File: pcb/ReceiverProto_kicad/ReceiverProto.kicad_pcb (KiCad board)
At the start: 4 copper layers, 75 x 50 mm, 65 parts, among them J1 Conn_01x09, J2 Conn_01x03, J3 Conn_01x04, J4 Conn_01x06, U11 ADM8660ARZ-REEL, U12 ADP7182AUJZ-1.8-R7, U13 ADA4807-1, U14 ADA4807-1, U15 ADA4807-1, U16 ADA4807-1, U4 AD7387BCPZ-RL7, U5 TLV9001IDCK, U6 TLV9001IDCK, U7 TPS79301DBVR

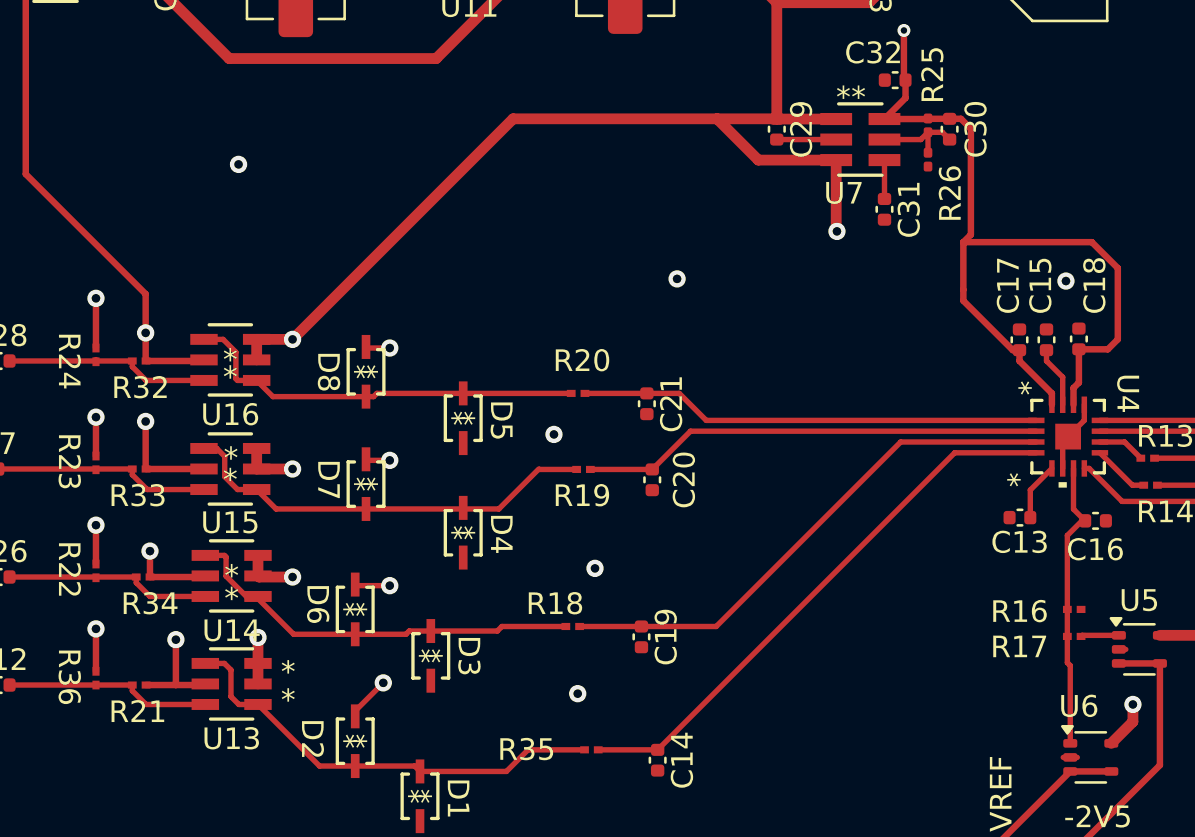
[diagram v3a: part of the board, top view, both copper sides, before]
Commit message: fixed all DRC errors except for silkscreen error.
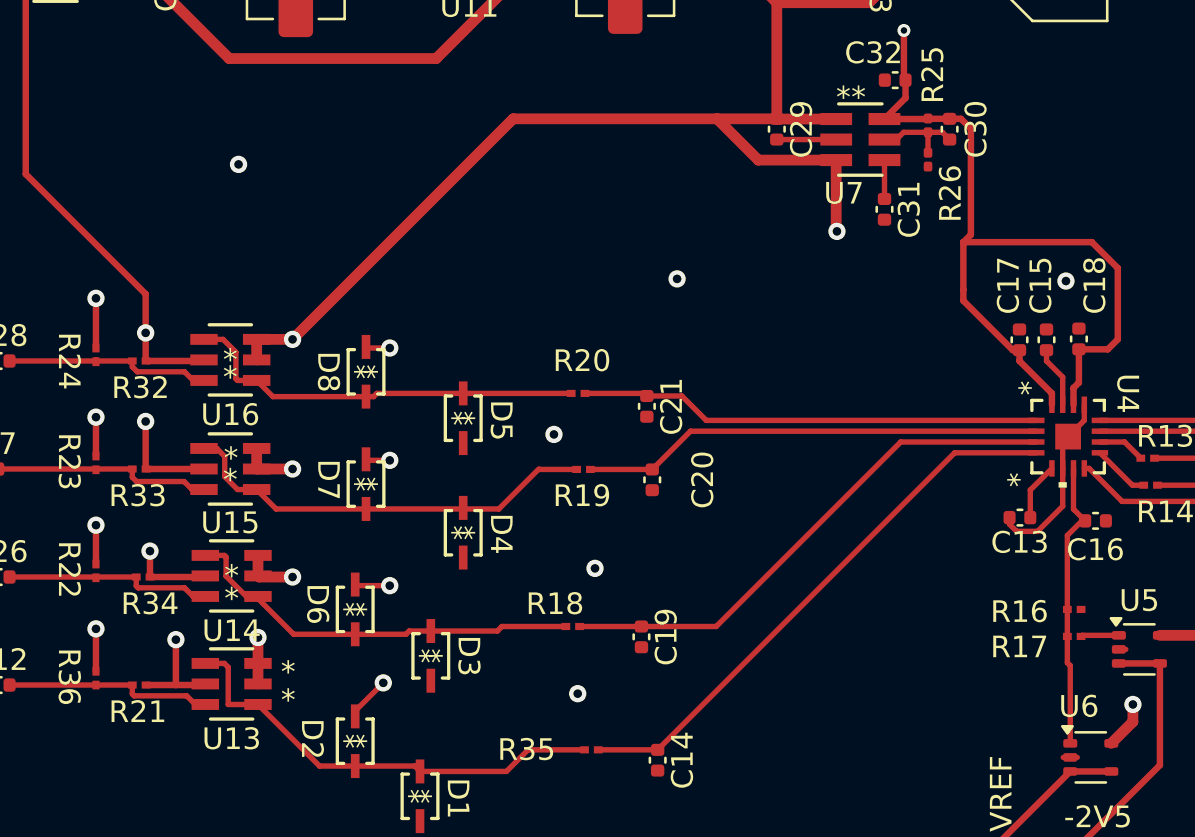
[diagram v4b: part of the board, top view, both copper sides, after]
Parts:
- moved C21 0.12 mm to (141.5, 115.6)
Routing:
- net GND: track 7.79 -> 12.9 mm
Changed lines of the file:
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@@
 			(psa4output no)
 			(plot_black_and_white yes)
+			(plotinvisibletext no)
 			(sketchpadsonfab no)
 			(plotpadnumbers no)
@@
 		(tags "capacitor")
 		(property "Reference" "C20"
-			(at 0 -1.5 90)
+			(at 0 -2.35 90)
 			(layer "F.SilkS")
 			(effects
@@
 		)
 		(property "Value" "330p"
-			(at 0.2 -1.75 90)
+			(at 0 -3.95 90)
 			(layer "F.Fab")
 			(effects
@@
 		)
 		(fp_text user "${REFERENCE}"
-			(at 0 0 90)
+			(at 0 -0.95 90)
 			(layer "F.Fab")
 			(effects
@@
 	(footprint "Capacitor_SMD:C_0402_1005Metric"
 		(layer "F.Cu")
-		(at 141.5 115.48 -90)
+		(at 141.5 115.6 -90)
 		(descr "Capacitor SMD 0402 (1005 Metric), square (rectangular) end terminal, IPC_7351 nominal, (Body size source: IPC-SM-782 page 76, https://www.pcb-3d.com/wordpress/wp-content/uploads/ipc-sm-782a_amendment_1_and_2.pdf), generated with kicad-footprint-generator")
 		(tags "capacitor")
@@
 	)
 	(segment
-		(start 117.6825 128.7651)
+		(start 116 128.5)
 		(end 117.6825 128.5)
 		(width 0.25)
@@
 	)
 	(segment
-		(start 116 128.5)
-		(end 117.6825 128.5)
+		(start 117.6825 128.9151)
+		(end 117.7674 129)
 		(width 0.25)
 		(layer "F.Cu")
@@
 	)
 	(segment
-		(start 121.0616 129.400002)
-		(end 118.317402 129.400002)
+		(start 117.7674 129)
+		(end 120.2 129)
+		(width 0.25)
+		(layer "F.Cu")
+		(net 2)
+	)
+	(segment
+		(start 120.600002 129.400002)
+		(end 120.2 129)
 		(width 0.25)
 		(layer "F.Cu")
@@
 	)
 	(segment
-		(start 118.317402 129.400002)
-		(end 117.6825 128.7651)
+		(start 121.0616 129.400002)
+		(end 120.600002 129.400002)
 		(width 0.25)
 		(layer "F.Cu")
@@
 	)
 	(segment
+		(start 117.6825 128.5)
+		(end 117.6825 128.9151)
+		(width 0.25)
+		(layer "F.Cu")
+		(net 2)
+	)
+	(segment
 		(start 159.25 119.473199)
 		(end 160.249999 118.4732)
@@
 	)
 	(segment
+		(start 159.586904 121.386)
+		(end 158.616001 121.386)
+		(width 0.25)
+		(layer "F.Cu")
+		(net 4)
+	)
+	(segment
 		(start 150.2648 103.25)
 		(end 147.5148 103.25)
@@
 	)
 	(segment
+		(start 160.75 118.4732)
+		(end 160.75 120.222904)
+		(width 0.25)
+		(layer "F.Cu")
+		(net 4)
+	)
+	(segment
+		(start 158.616001 121.386)
+		(end 158.29 121.059999)
+		(width 0.25)
+		(layer "F.Cu")
+		(net 4)
+	)
+	(segment
 		(start 161.750001 116.249999)
 		(end 161 117)
@@
 	)
 	(segment
+		(start 158.29 121.059999)
+		(end 158.29 120.75)
+		(width 0.25)
+		(layer "F.Cu")
+		(net 4)
+	)
+	(segment
 		(start 161.750001 115.5268)
 		(end 161.750001 116.249999)
@@
 	)
 	(segment
+		(start 160.75 120.222904)
+		(end 159.586904 121.386)
+		(width 0.25)
+		(layer "F.Cu")
+		(net 4)
+	)
+	(segment
 		(start 160.75 117.25)
 		(end 161 117)
@@
 	)
 	(segment
+		(start 138.635 115)
+		(end 141.38 115)
+		(width 0.25)
+		(layer "F.Cu")
+		(net 11)
+	)
+	(segment
 		(start 144.249999 116.249999)
-		(end 143 115)
+		(end 143.12 115.12)
 		(width 0.25)
 		(layer "F.Cu")
@@
 	)
 	(segment
-		(start 143 115)
-		(end 141.5 115)
+		(start 143.12 115.12)
+		(end 141.5 115.12)
 		(width 0.25)
 		(layer "F.Cu")
@@
 	)
 	(segment
-		(start 138.635 115)
-		(end 141.5 115)
+		(start 141.38 115)
+		(end 141.5 115.12)
 		(width 0.25)
 		(layer "F.Cu")
@@
 	)
 	(segment
+		(start 117.865 123.5)
+		(end 117.865 123.9151)
+		(width 0.25)
+		(layer "F.Cu")
+		(net 16)
+	)
+	(segment
 		(start 115.965 123.5)
 		(end 116 123.535)
@@
 	)
 	(segment
-		(start 118.499902 124.400002)
-		(end 117.865 123.7651)
+		(start 120.1 124)
+		(end 120.500002 124.400002)
 		(width 0.25)
 		(layer "F.Cu")
@@
 	)
 	(segment
+		(start 117.9499 124)
+		(end 120.1 124)
+		(width 0.25)
+		(layer "F.Cu")
+		(net 16)
+	)
+	(segment
 		(start 116.035 123.5)
 		(end 116 123.535)
@@
 	)
 	(segment
-		(start 121.0616 124.400002)
-		(end 118.499902 124.400002)
+		(start 117.865 123.9151)
+		(end 117.9499 124)
 		(width 0.25)
 		(layer "F.Cu")
@@
 	)
 	(segment
-		(start 117.865 123.5)
-		(end 116.035 123.5)
+		(start 120.500002 124.400002)
+		(end 121.0616 124.400002)
 		(width 0.25)
 		(layer "F.Cu")
@@
 	)
 	(segment
-		(start 117.865 123.7651)
-		(end 117.865 123.5)
+		(start 117.865 123.5)
+		(end 116.035 123.5)
 		(width 0.25)
 		(layer "F.Cu")
@@
 	)
 	(segment
-		(start 118.367401 119.450001)
-		(end 117.6825 118.7651)
+		(start 117.6825 118.8853)
+		(end 117.8772 119.08)
+		(width 0.25)
+		(layer "F.Cu")
+		(net 19)
+	)
+	(segment
+		(start 117.8772 119.08)
+		(end 120.08 119.08)
 		(width 0.25)
 		(layer "F.Cu")
@@
 	)
 	(segment
-		(start 121 119.450001)
-		(end 118.367401 119.450001)
+		(start 120.08 119.08)
+		(end 120.450001 119.450001)
 		(width 0.25)
 		(layer "F.Cu")
@@
 	)
 	(segment
-		(start 117.6825 118.7651)
-		(end 117.6825 118.5)
+		(start 120.450001 119.450001)
+		(end 121 119.450001)
+		(width 0.25)
+		(layer "F.Cu")
+		(net 19)
+	)
+	(segment
+		(start 117.6825 118.5)
+		(end 117.6825 118.8853)
 		(width 0.25)
 		(layer "F.Cu")
@@
 	)
 	(segment
-		(start 117.6825 113.7651)
-		(end 117.6825 113.5)
+		(start 120.500002 114.400002)
+		(end 121 114.400002)
 		(width 0.25)
 		(layer "F.Cu")
@@
 	)
 	(segment
-		(start 121 114.400002)
-		(end 118.317402 114.400002)
+		(start 117.6825 113.5)
+		(end 117.6825 113.7651)
+		(width 0.25)
+		(layer "F.Cu")
+		(net 21)
+	)
+	(segment
+		(start 117.9174 114)
+		(end 120.1 114)
 		(width 0.25)
 		(layer "F.Cu")
@@
 	)
 	(segment
-		(start 118.317402 114.400002)
-		(end 117.6825 113.7651)
+		(start 120.1 114)
+		(end 120.500002 114.400002)
 		(width 0.25)
 		(layer "F.Cu")
@@
 	)
 	(segment
+		(start 117.6825 113.7651)
+		(end 117.9174 114)
+		(width 0.25)
+		(layer "F.Cu")
+		(net 21)
+	)
+	(segment
 		(start 147.5148 96.9148)
 		(end 147.5148 102.29)
@@
 	)
 	(segment
-		(start 155.1798 102.915)
-		(end 155.5148 103.25)
+		(start 153.05 103.25)
+		(end 152.5 103.25)
 		(width 0.25)
 		(layer "F.Cu")
@@
 	(segment
 		(start 154.5148 102.915)
-		(end 155.1798 102.915)
+		(end 153.385 102.915)
 		(width 0.25)
 		(layer "F.Cu")
@@
 	)
 	(segment
-		(start 152.5 103.25)
-		(end 154.1798 103.25)
+		(start 155.1798 102.915)
+		(end 155.5148 103.25)
 		(width 0.25)
 		(layer "F.Cu")
@@
 	)
 	(segment
-		(start 154.1798 103.25)
-		(end 154.5148 102.915)
+		(start 154.5148 102.915)
+		(end 155.1798 102.915)
+		(width 0.25)
+		(layer "F.Cu")
+		(net 23)
+	)
+	(segment
+		(start 153.385 102.915)
+		(end 153.05 103.25)
 		(width 0.25)
 		(layer "F.Cu")
@@
 	)
 	(segment
-		(start 128 132.250001)
-		(end 126.349999 132.250001)
+		(start 123.5 129.400002)
+		(end 122.122602 129.400002)
 		(width 0.25)
 		(layer "F.Cu")
@@
 	)
 	(segment
-		(start 122.25 129.035002)
-		(end 122.615 129.400002)
+		(start 128 132.250001)
+		(end 126.349999 132.250001)
 		(width 0.25)
 		(layer "F.Cu")
@@
 	)
 	(segment
-		(start 135 132.5)
-		(end 136 131.5)
+		(start 122.122602 129.400002)
+		(end 122.122602 127.676002)
 		(width 0.25)
 		(layer "F.Cu")
@@
 	)
 	(segment
-		(start 122.25 127.8034)
-		(end 122.25 129.035002)
+		(start 135 132.5)
+		(end 136 131.5)
 		(width 0.25)
 		(layer "F.Cu")
@@
 	)
 	(segment
-		(start 131 132.5)
-		(end 135 132.5)
+		(start 121.9466 127.5)
+		(end 121.0616 127.5)
 		(width 0.25)
 		(layer "F.Cu")
@@
 	)
 	(segment
-		(start 122.615 129.400002)
-		(end 123.5 129.400002)
+		(start 131 132.5)
+		(end 135 132.5)
 		(width 0.25)
 		(layer "F.Cu")
@@
 	)
 	(segment
-		(start 121.0616 127.5)
+		(start 122.122602 127.676002)
 		(end 121.9466 127.5)
 		(width 0.25)
 		(layer "F.Cu")
-		(net 36)
-	)
-	(segment
-		(start 121.9466 127.5)
-		(end 122.25 127.8034)
-		(width 0.25)
-		(layer "F.Cu")

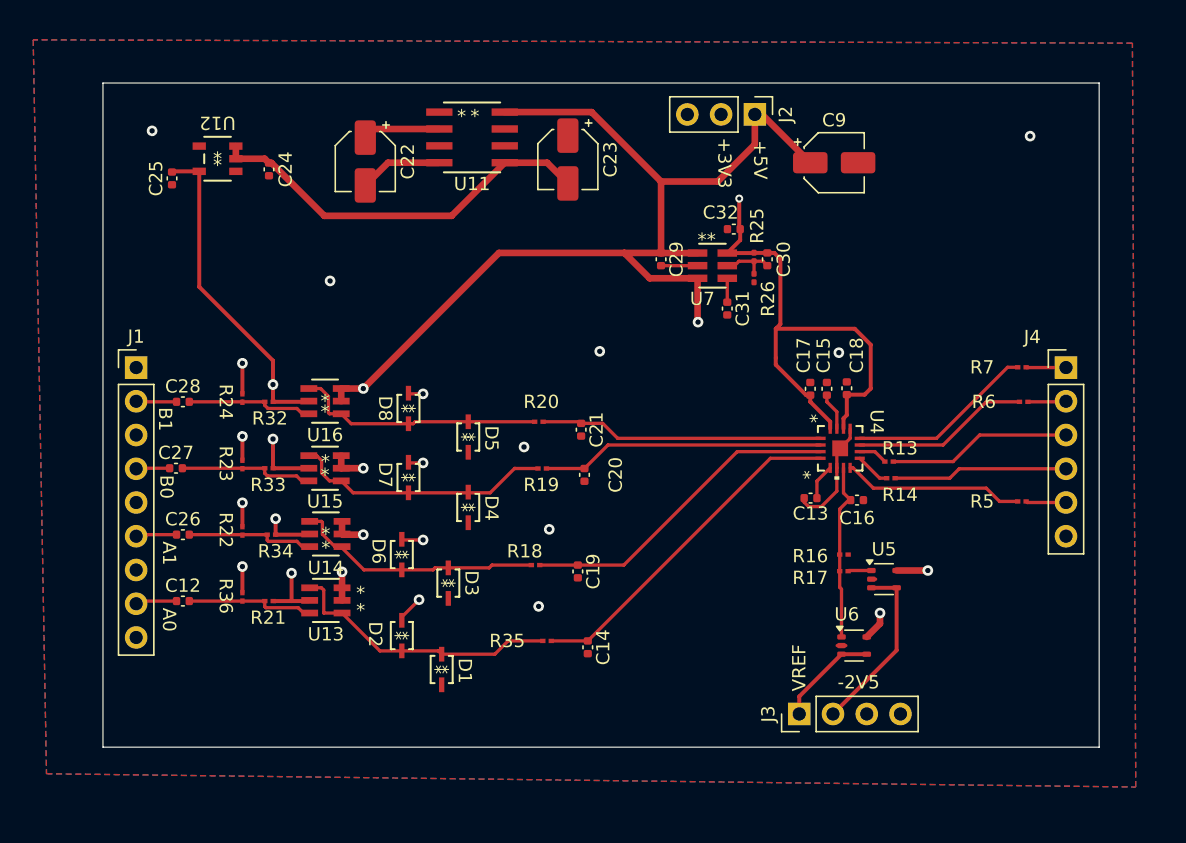
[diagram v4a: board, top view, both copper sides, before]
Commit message: add labels for adc digital header; move asterisks to indicate pin 1's
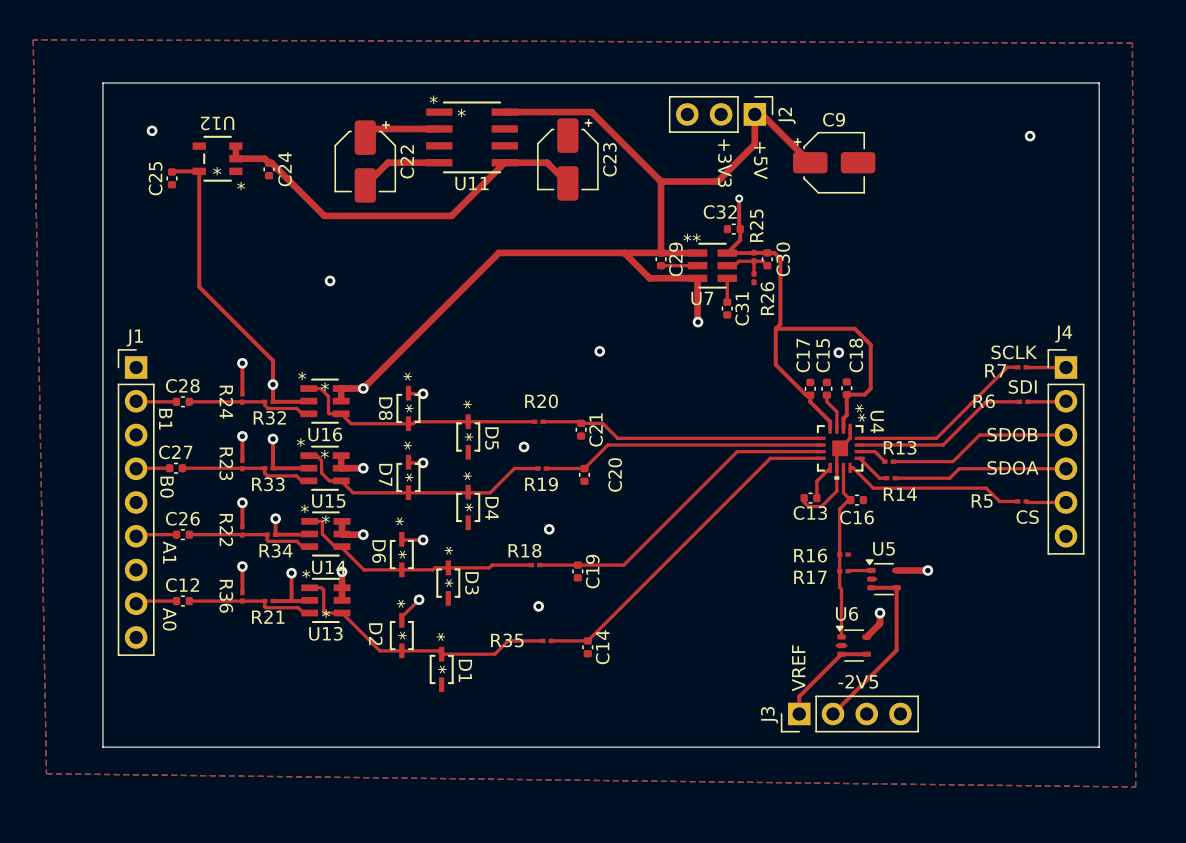
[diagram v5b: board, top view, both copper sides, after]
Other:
- board text added: "CS"
- board text added: "SCLK"
- board text added: "SDI"
- board text added: "SDOA"
- board text added: "SDOB"
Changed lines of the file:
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@@
 			(psa4output no)
 			(plot_black_and_white yes)
-			(plotinvisibletext no)
 			(sketchpadsonfab no)
 			(plotpadnumbers no)
@@
 		)
 		(fp_text user "*"
-			(at 0 0.799999 0)
+			(at -1.7192 -1.650001 0)
 			(layer "F.SilkS")
 			(effects
@@
 		)
 		(fp_text user "*"
-			(at 0 0 0)
+			(at 0 -0.850001 0)
 			(unlocked yes)
 			(layer "F.SilkS")
@@
 		(tags "RC0201FR-07100RL ")
 		(property "Reference" "R7"
-			(at -3 0 0)
+			(at -1.9825 0.3 0)
 			(unlocked yes)
 			(layer "F.SilkS")
@@
 		)
 		(fp_text user "*"
-			(at 0 0 90)
+			(at 0 -0.3 90)
 			(layer "F.SilkS")
 			(effects
@@
 		)
 		(fp_text user "*"
-			(at 0 0 270)
+			(at -2.5 0.4 270)
 			(unlocked yes)
 			(layer "F.SilkS")
@@
 		)
 		(fp_text user "*"
-			(at -0.7824 -1.95 0)
+			(at -1.8824 -1.85 0)
 			(unlocked yes)
 			(layer "F.SilkS")
@@
 		)
 		(fp_text user "*"
-			(at -0.0824 -1.95 0)
+			(at -1.1824 -1.85 0)
 			(layer "F.SilkS")
 			(effects
@@
 		(tags "ADA4807-1ARJZ-R2 ")
 		(property "Reference" "U15"
-			(at 0 2.5 0)
+			(at 0.2808 2.5 0)
 			(unlocked yes)
 			(layer "F.SilkS")
@@
 		)
 		(fp_text user "*"
-			(at 0 0.5 0)
+			(at -1.8192 -1.7 0)
 			(unlocked yes)
 			(layer "F.SilkS")
@@
 		)
 		(fp_text user "*"
-			(at 0.0308 -0.5 0)
+			(at -0.0192 -0.8 0)
 			(layer "F.SilkS")
 			(effects
@@
 		)
 		(fp_text user "*"
-			(at 0 0 270)
+			(at -2.45 0.2 270)
 			(unlocked yes)
 			(layer "F.SilkS")
@@
 		)
 		(fp_text user "*"
-			(at 0 0 90)
+			(at 0 -0.3 90)
 			(layer "F.SilkS")
 			(effects
@@
 		)
 		(fp_text user "*"
-			(at 0 0 180)
+			(at 0.02795 -0.699999 180)
 			(unlocked yes)
 			(layer "F.SilkS")
@@
 		)
 		(fp_text user "*"
-			(at 0 0 0)
+			(at -1.77205 -2.299999 0)
 			(layer "F.SilkS")
 			(effects
@@
 		)
 		(fp_text user "*"
-			(at 0 0 270)
+			(at -2.4 0.3 270)
 			(unlocked yes)
 			(layer "F.SilkS")
@@
 		)
 		(fp_text user "*"
-			(at 0 0 90)
+			(at 0 -0.3 90)
 			(layer "F.SilkS")
 			(effects
@@
 		)
 		(fp_text user "*"
-			(at 0.2138 -1.595 0)
+			(at -2.8862 -2.595 0)
 			(layer "F.SilkS")
 			(effects
@@
 		)
 		(fp_text user "*"
-			(at 0 0 270)
+			(at -2.45 0.3 270)
 			(unlocked yes)
 			(layer "F.SilkS")
@@
 		)
 		(fp_text user "*"
-			(at 0 0 90)
+			(at 0 -0.3 90)
 			(layer "F.SilkS")
 			(effects
@@
 		)
 		(fp_text user "*"
-			(at 2 2.75 270)
+			(at -2.3 -1.4 270)
 			(unlocked yes)
 			(layer "F.SilkS")
@@
 		)
 		(fp_text user "*"
-			(at -2.25 1.75 90)
+			(at -3 -1.7 90)
 			(layer "F.SilkS")
 			(effects
@@
 		)
 		(fp_text user "*"
-			(at 0 0 90)
+			(at 0 -0.3 90)
 			(layer "F.SilkS")
 			(effects
@@
 		)
 		(fp_text user "*"
-			(at 0 0 270)
+			(at -2.4 0.3 270)
 			(unlocked yes)
 			(layer "F.SilkS")
@@
 		)
 		(fp_text user "*"
-			(at 0 0 270)
+			(at -2.35 0.3 270)
 			(unlocked yes)
 			(layer "F.SilkS")
@@
 		)
 		(fp_text user "*"
-			(at 0 0 90)
+			(at 0 -0.3 90)
 			(layer "F.SilkS")
 			(effects
@@
 		)
 		(fp_text user "*"
-			(at 0 0 90)
+			(at 0 -0.3 90)
 			(layer "F.SilkS")
 			(effects
@@
 		)
 		(fp_text user "*"
-			(at 0 0 270)
+			(at -2.400001 0.3 270)
 			(unlocked yes)
 			(layer "F.SilkS")
@@
 		)
 		(fp_text user "*"
-			(at 2.6192 -0.550001 0)
+			(at -1.4808 -1.750001 0)
 			(unlocked yes)
 			(layer "F.SilkS")
@@
 		)
 		(fp_text user "*"
-			(at 2.6192 0.749999 0)
+			(at 0.0192 1.249999 0)
 			(layer "F.SilkS")
 			(effects
@@
 		(tags "ADA4807-1ARJZ-R2 ")
 		(property "Reference" "U14"
-			(at 0 2.549999 0)
+			(at 0.2192 2.549999 0)
 			(unlocked yes)
 			(layer "F.SilkS")
@@
 		)
 		(fp_text user "*"
-			(at 0 1.049999 0)
+			(at -1.5808 -1.650001 0)
 			(layer "F.SilkS")
 			(effects
@@
 		)
 		(fp_text user "*"
-			(at 0 0 0)
+			(at 0 -0.850001 0)
 			(unlocked yes)
 			(layer "F.SilkS")
@@
 		)
 		(fp_text user "*"
-			(at 0 0 90)
+			(at 0 -0.3 90)
 			(layer "F.SilkS")
 			(effects
@@
 		)
 		(fp_text user "*"
-			(at 0 0 270)
+			(at -2.45 0.3 270)
 			(unlocked yes)
 			(layer "F.SilkS")
@@
 		(tags "Through hole pin header THT 1x06 2.54mm single row")
 		(property "Reference" "J4"
-			(at -2.5362 -2.3 0)
+			(at -0.1 -2.62 0)
 			(layer "F.SilkS")
 			(effects
@@
 		(layer "Edge.Cuts")
 	)
+	(gr_text "SDOA"
+		(at 172 119.1 0)
+		(layer "F.SilkS")
+		(effects
+			(font
+				(size 1 1)
+				(thickness 0.153)
+			)
+			(justify left bottom)
+		)
+	)
 	(gr_text "B0"
 		(at 109.7 119 270)
@@
 		)
 	)
+	(gr_text "CS"
+		(at 174.2 122.8 0)
+		(layer "F.SilkS")
+		(effects
+			(font
+				(size 1 1)
+				(thickness 0.153)
+			)
+			(justify left bottom)
+		)
+	)
 	(gr_text "-2V5"
 		(at 160.8 135.2 0)
@@
 		)
 	)
+	(gr_text "SDOB"
+		(at 172 116.6 0)
+		(layer "F.SilkS")
+		(effects
+			(font
+				(size 1 1)
+				(thickness 0.153)
+			)
+			(justify left bottom)
+		)
+	)
 	(gr_text "VREF"
 		(at 158.5 135.3 90)
@@
 		)
 	)
+	(gr_text "SCLK"
+		(at 172.3 110.4 0)
+		(layer "F.SilkS")
+		(effects
+			(font
+				(size 1 1)
+				(thickness 0.153)
+			)
+			(justify left bottom)
+		)
+	)
 	(gr_text "A0"
 		(at 109.9 129 270)
 		(layer "F.SilkS")
 		(effects
+			(font
+				(size 1 1)
+				(thickness 0.153)
+			)
+			(justify left bottom)
+		)
+	)
+	(gr_text "SDI"
+		(at 173.6 113 0)
+		(layer "F.SilkS")
+		(effects
